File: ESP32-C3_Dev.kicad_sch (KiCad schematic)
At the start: 26 parts, among them J1 Conn_01x09_Pin, J2 DX07S024JJ2R1300, J3 Conn_01x09_Pin, SW1 SW_MEC_5G, SW2 SW_MEC_5G, U1 ESP32-C3-WROOM-02, U2 AMS1117-3.3

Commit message: wip
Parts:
- removed C1, C2, C4: 10u 25V, Capacitor_SMD:C_0603_1608Metric, symbol _PS_LIB:C_0603
- removed C3, C5, C7, C8: 100n, Capacitor_SMD:C_0603_1608Metric, symbol _PS_LIB:C_0603
- removed D1, D3, D4: LESD5D5.0CT1G, Diode_SMD:D_SOD-523, symbol Diode:ESD5Zxx
- removed D2: 1N5819WS, Diode_SMD:D_SOD-323, symbol Diode:1N5819WS
- removed D5, D6: LED, LED_SMD:LED_0603_1608Metric, symbol _PS_LIB:LED
- removed J1, J3: Conn_01x09_Pin, Connector_PinHeader_2.54mm:PinHeader_1x09_P2.54mm_Vertical, symbol Connector:Conn_01x09_Pin
- removed J2: DX07S024JJ2R1300, Connector_USB:USB_C_Receptacle_GCT_USB4105-xx-A_16P_TopMnt_Horizontal, symbol DX07S024JJ2R1300:DX07S024JJ2R1300
- removed R1, R2, R3, R6: 5k1, Resistor_SMD:R_0603_1608Metric, symbol _PS_LIB:R_0603
- removed R4, R5: 10k, Resistor_SMD:R_0603_1608Metric, symbol _PS_LIB:R_0603
- removed SW1, SW2: SW_MEC_5G, _PS_LIB_PCB:Xunpu TS-1088, symbol _PS_LIB:SW_MEC_5G
- removed U1: ESP32-C3-WROOM-02, RF_Module:ESP32-C3-WROOM-02, symbol RF_Module:ESP32-C3-WROOM-02
- removed U2: AMS1117-3.3, Package_TO_SOT_SMD:SOT-223-3_TabPin2, symbol Regulator_Linear:AMS1117-3.3
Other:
- added sheet Controller (controller.kicad_sch)
- added sheet PT100 (pt100.kicad_sch)
- added sheet Power Supply (powersupply.kicad_sch)

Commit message: wip schematic
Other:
- sheet Controller ports: added CHARGING, READY, UBAT; removed none
- sheet Power Supply ports: added CHARGING, READY, UBAT; removed none
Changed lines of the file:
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@@
+	(wire
+		(pts
+			(xy 135.89 54.61) (xy 147.32 54.61)
+		)
+		(stroke
+			(width 0)
+			(type default)
+		)
+	)
+	(wire
+		(pts
+			(xy 135.89 64.77) (xy 147.32 64.77)
+		)
+		(stroke
+			(width 0)
+			(type default)
+		)
+	)
 	(wire
 		(pts
@@
 	(wire
 		(pts
-			(xy 135.89 55.88) (xy 147.32 55.88)
+			(xy 135.89 57.15) (xy 147.32 57.15)
 		)
 		(stroke
@@
 		(pts
 			(xy 135.89 85.09) (xy 147.32 85.09)
+		)
+		(stroke
+			(width 0)
+			(type default)
+		)
+	)
+	(wire
+		(pts
+			(xy 135.89 62.23) (xy 147.32 62.23)
 		)
 		(stroke
@@
 		)
 		(pin "USB+" bidirectional
-			(at 147.32 55.88 180)
+			(at 147.32 54.61 180)
 			(effects
 				(font
@@
 		)
 		(pin "USB-" bidirectional
+			(at 147.32 57.15 180)
+			(effects
+				(font
+					(size 1.27 1.27)
+				)
+				(justify left)
+			)
+		)
+		(pin "SHDN2" output
+			(at 147.32 85.09 180)
+			(effects
+				(font
+					(size 1.27 1.27)
+				)
+				(justify left)
+			)
+		)
+		(pin "SHDN1" output
+			(at 147.32 80.01 180)
+			(effects
+				(font
+					(size 1.27 1.27)
+				)
+				(justify left)
+			)
+		)
+		(pin "PT100_1" input
+			(at 147.32 77.47 180)
+			(effects
+				(font
+					(size 1.27 1.27)
+				)
+				(justify left)
+			)
+		)
+		(pin "PT100_2" input
+			(at 147.32 82.55 180)
+			(effects
+				(font
+					(size 1.27 1.27)
+				)
+				(justify left)
+			)
+		)
+		(pin "READY" input
+			(at 147.32 62.23 180)
+			(effects
+				(font
+					(size 1.27 1.27)
+				)
+				(justify left)
+			)
+		)
+		(pin "CHARGING" input
 			(at 147.32 59.69 180)
 			(effects
@@
 			)
 		)
-		(pin "SHDN1" bidirectional
-			(at 147.32 80.01 180)
-			(effects
-				(font
-					(size 1.27 1.27)
-				)
-				(justify left)
-			)
-		)
-		(pin "PT100_2" bidirectional
-			(at 147.32 82.55 180)
-			(effects
-				(font
-					(size 1.27 1.27)
-				)
-				(justify left)
-			)
-		)
-		(pin "PT100_1" bidirectional
-			(at 147.32 77.47 180)
-			(effects
-				(font
-					(size 1.27 1.27)
-				)
-				(justify left)
-			)
-		)
-		(pin "SHDN2" bidirectional
-			(at 147.32 85.09 180)
+		(pin "UBAT" input
+			(at 147.32 64.77 180)
 			(effects
 				(font
@@
 	(sheet
 		(at 107.95 52.07)
-		(size 27.94 12.7)
+		(size 27.94 15.24)
 		(exclude_from_sim no)
 		(in_bom yes)
@@
 		)
 		(property "Sheetfile" "powersupply.kicad_sch"
-			(at 107.95 65.3546 0)
+			(at 107.95 67.8946 0)
 			(effects
 				(font
@@
 		)
 		(pin "USB+" bidirectional
-			(at 135.89 55.88 0)
+			(at 135.89 54.61 0)
 			(effects
 				(font
@@
 		)
 		(pin "USB-" bidirectional
+			(at 135.89 57.15 0)
+			(effects
+				(font
+					(size 1.27 1.27)
+				)
+				(justify right)
+			)
+		)
+		(pin "CHARGING" output
 			(at 135.89 59.69 0)
 			(effects
 				(font
+					(size 1.27 1.27)
+				)
+				(justify right)
+			)
+		)
+		(pin "READY" output
+			(at 135.89 62.23 0)
+			(effects
+				(font
+					(size 1.27 1.27)
+				)
+				(justify right)
+			)
+		)
+		(pin "UBAT" output
+			(at 135.89 64.77 0)
+			(effects
+				(font

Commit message: wip
lcsc part numbers
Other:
- sheet Power Supply ports: added SHDN1; removed none
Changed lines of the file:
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@@
 	(generator_version "9.0")
 	(paper "A4")
+	(junction
+		(at 143.51 80.01)
+		(diameter 0)
+		(color 0 0 0 0)
+	)
 	(wire
 		(pts
@@
 	(wire
 		(pts
-			(xy 135.89 80.01) (xy 147.32 80.01)
+			(xy 135.89 80.01) (xy 143.51 80.01)
+		)
+		(stroke
+			(width 0)
+			(type default)
+		)
+	)
+	(wire
+		(pts
+			(xy 135.89 67.31) (xy 143.51 67.31)
 		)
 		(stroke
@@
 	(wire
 		(pts
+			(xy 143.51 67.31) (xy 143.51 80.01)
+		)
+		(stroke
+			(width 0)
+			(type default)
+		)
+	)
+	(wire
+		(pts
 			(xy 135.89 64.77) (xy 147.32 64.77)
 		)
@@
 		(pts
 			(xy 135.89 85.09) (xy 147.32 85.09)
+		)
+		(stroke
+			(width 0)
+			(type default)
+		)
+	)
+	(wire
+		(pts
+			(xy 143.51 80.01) (xy 147.32 80.01)
 		)
 		(stroke
@@
 			)
 		)
-		(pin "PT100_1" bidirectional
+		(pin "PT100_1" output
 			(at 135.89 77.47 0)
 			(effects
@@
 			)
 		)
-		(pin "SHDN1" bidirectional
+		(pin "SHDN1" input
 			(at 135.89 80.01 0)
 			(effects
@@
 			)
 		)
-		(pin "PT100_2" bidirectional
+		(pin "PT100_2" output
 			(at 135.89 82.55 0)
 			(effects
@@
 			)
 		)
-		(pin "SHDN2" bidirectional
+		(pin "SHDN2" input
 			(at 135.89 85.09 0)
 			(effects
@@
 	(sheet
 		(at 107.95 52.07)
-		(size 27.94 15.24)
+		(size 27.94 16.51)
 		(exclude_from_sim no)
 		(in_bom yes)
@@
 		)
 		(property "Sheetfile" "powersupply.kicad_sch"
-			(at 107.95 67.8946 0)
+			(at 107.95 69.1646 0)
 			(effects
 				(font
@@
 			(effects
 				(font
+					(size 1.27 1.27)
+				)
+				(justify right)
+			)
+		)
+		(pin "SHDN1" input
+			(at 135.89 67.31 0)
+			(effects
+				(font

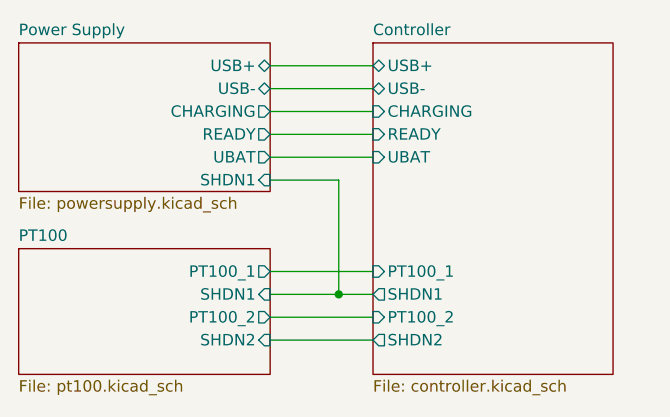
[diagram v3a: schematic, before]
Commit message: level shift for op en added
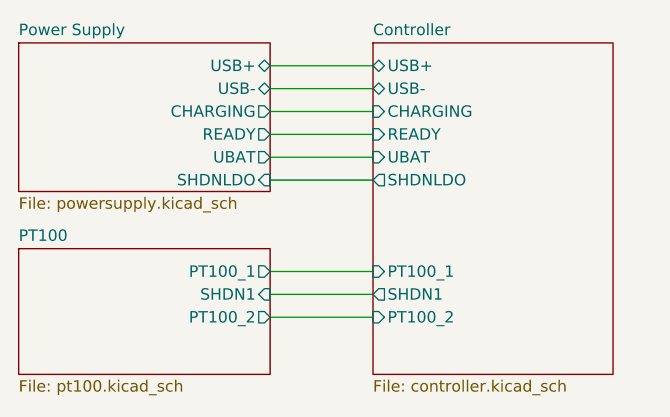
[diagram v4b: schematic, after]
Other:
- sheet Controller ports: added SHDNLDO; removed SHDN2
- sheet PT100 ports: added none; removed SHDN2
- sheet Power Supply ports: added SHDNLDO; removed SHDN1
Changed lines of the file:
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@@
 	(generator_version "9.0")
 	(paper "A4")
-	(junction
-		(at 143.51 80.01)
-		(diameter 0)
-		(color 0 0 0 0)
-	)
 	(wire
 		(pts
@@
 	(wire
 		(pts
-			(xy 135.89 80.01) (xy 143.51 80.01)
-		)
-		(stroke
-			(width 0)
-			(type default)
-		)
-	)
-	(wire
-		(pts
-			(xy 135.89 67.31) (xy 143.51 67.31)
+			(xy 135.89 67.31) (xy 147.32 67.31)
 		)
 		(stroke
@@
 	(wire
 		(pts
-			(xy 143.51 67.31) (xy 143.51 80.01)
-		)
-		(stroke
-			(width 0)
-			(type default)
-		)
-	)
-	(wire
-		(pts
 			(xy 135.89 64.77) (xy 147.32 64.77)
 		)
@@
 	(wire
 		(pts
-			(xy 135.89 85.09) (xy 147.32 85.09)
-		)
-		(stroke
-			(width 0)
-			(type default)
-		)
-	)
-	(wire
-		(pts
-			(xy 143.51 80.01) (xy 147.32 80.01)
+			(xy 135.89 80.01) (xy 147.32 80.01)
 		)
 		(stroke
@@
 			)
 		)
-		(pin "SHDN2" output
-			(at 147.32 85.09 180)
-			(effects
-				(font
-					(size 1.27 1.27)
-				)
-				(justify left)
-			)
-		)
 		(pin "SHDN1" output
 			(at 147.32 80.01 180)
@@
 		(pin "UBAT" input
 			(at 147.32 64.77 180)
+			(effects
+				(font
+					(size 1.27 1.27)
+				)
+				(justify left)
+			)
+		)
+		(pin "SHDNLDO" output
+			(at 147.32 67.31 180)
 			(effects
 				(font
@@
 			)
 		)
-		(pin "SHDN2" input
-			(at 135.89 85.09 0)
-			(effects
-				(font
-					(size 1.27 1.27)
-				)
-				(justify right)
-			)
-		)
 		(instances
 			(project "ESP32-C3_Dev"
@@
 			)
 		)
-		(pin "SHDN1" input
+		(pin "SHDNLDO" input
 			(at 135.89 67.31 0)
 			(effects
